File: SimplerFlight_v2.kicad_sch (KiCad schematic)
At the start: 18 parts

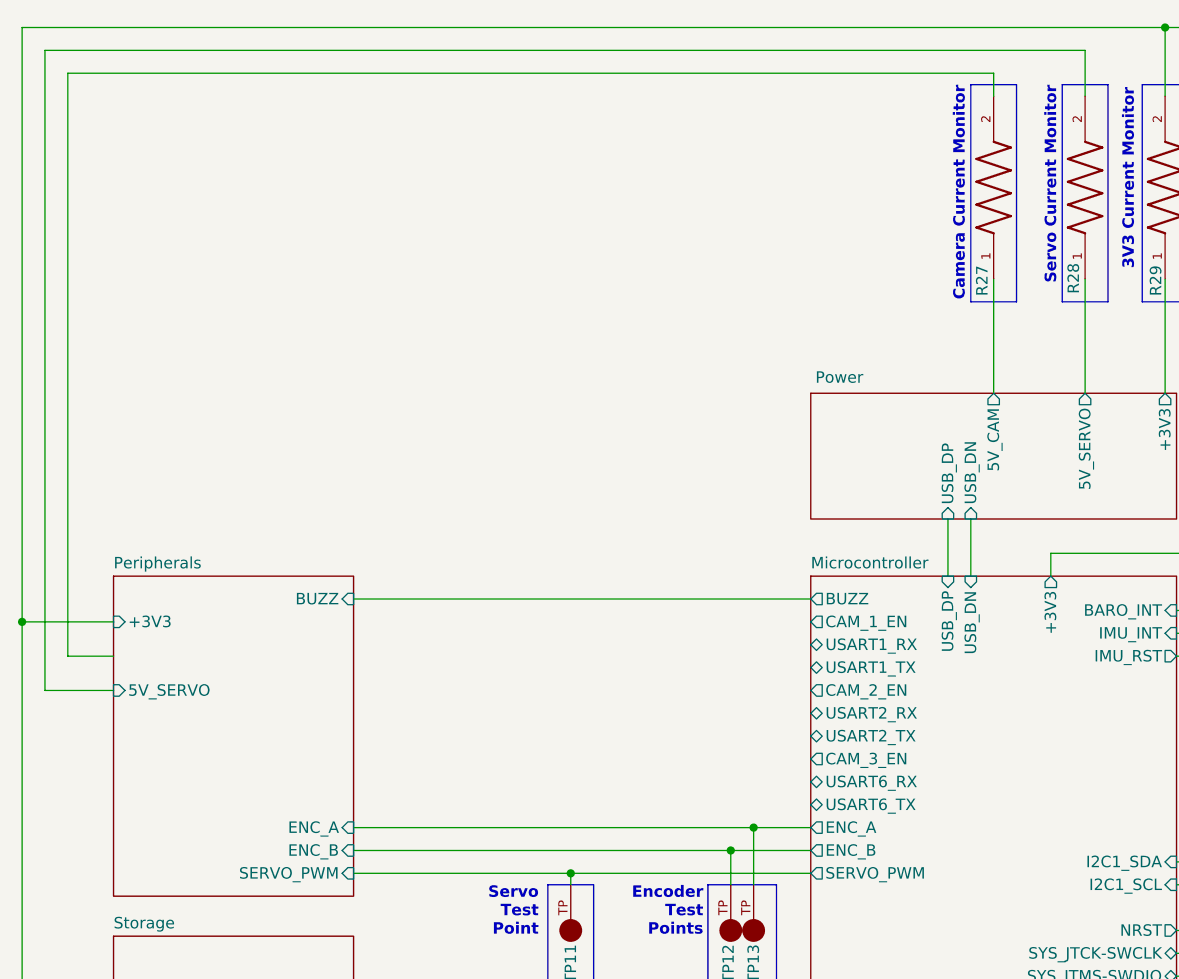
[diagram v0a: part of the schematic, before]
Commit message: remove redundant current sensing
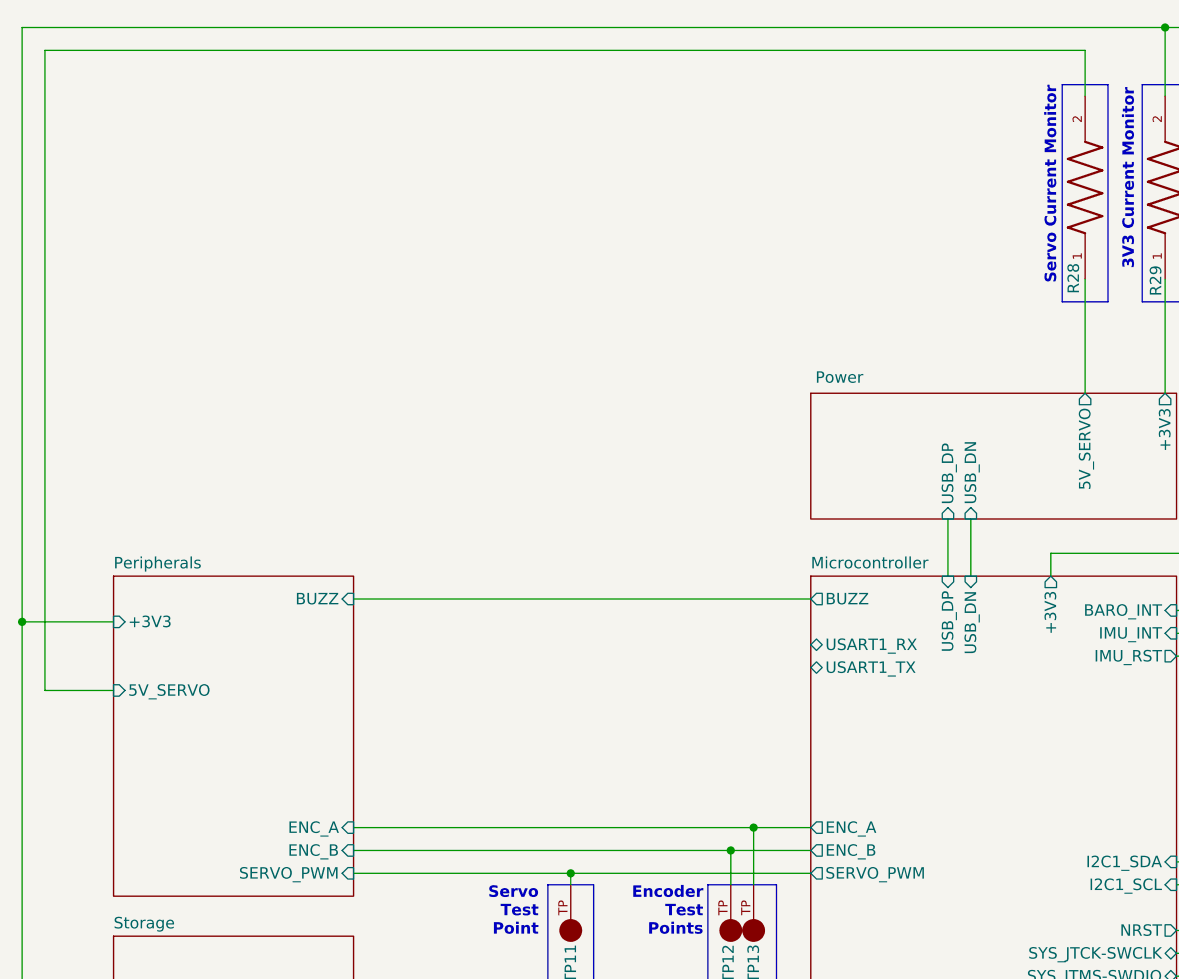
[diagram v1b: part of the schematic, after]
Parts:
- removed R27: CSRN2512FKR500, CSRN2512FKR500:RESC6331X70N, symbol CSRN2512FKR500:CSRN2512FKR500
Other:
- sheet Microcontroller ports: added none; removed CAM_1_EN, CAM_2_EN, CAM_3_EN, USART2_RX, USART2_TX, USART6_RX, USART6_TX
- sheet Power ports: added none; removed 5V_CAM
- note removed: "Camera Current Monitor"
